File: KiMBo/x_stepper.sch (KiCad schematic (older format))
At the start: 11 parts

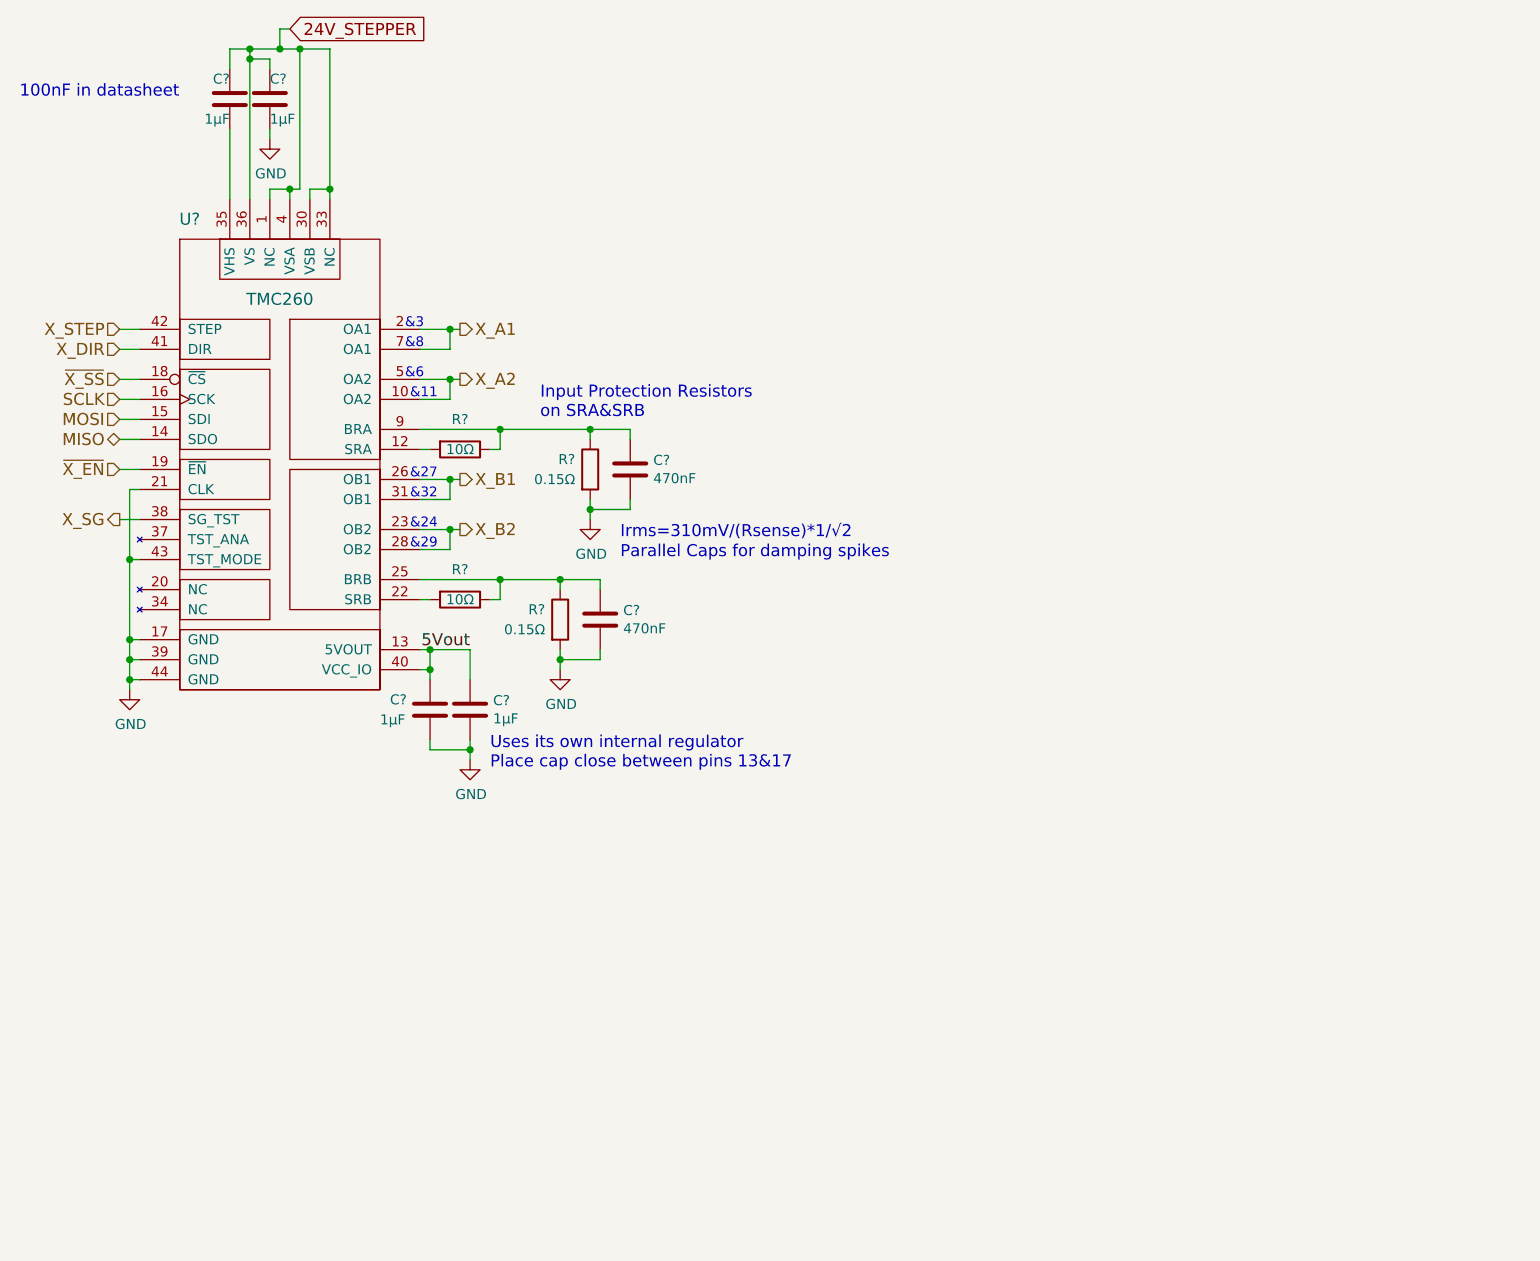
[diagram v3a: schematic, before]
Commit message: Update the fixed Vain voltage and begin placing connectors at the highest level (root) of the hierarchical sheet structure
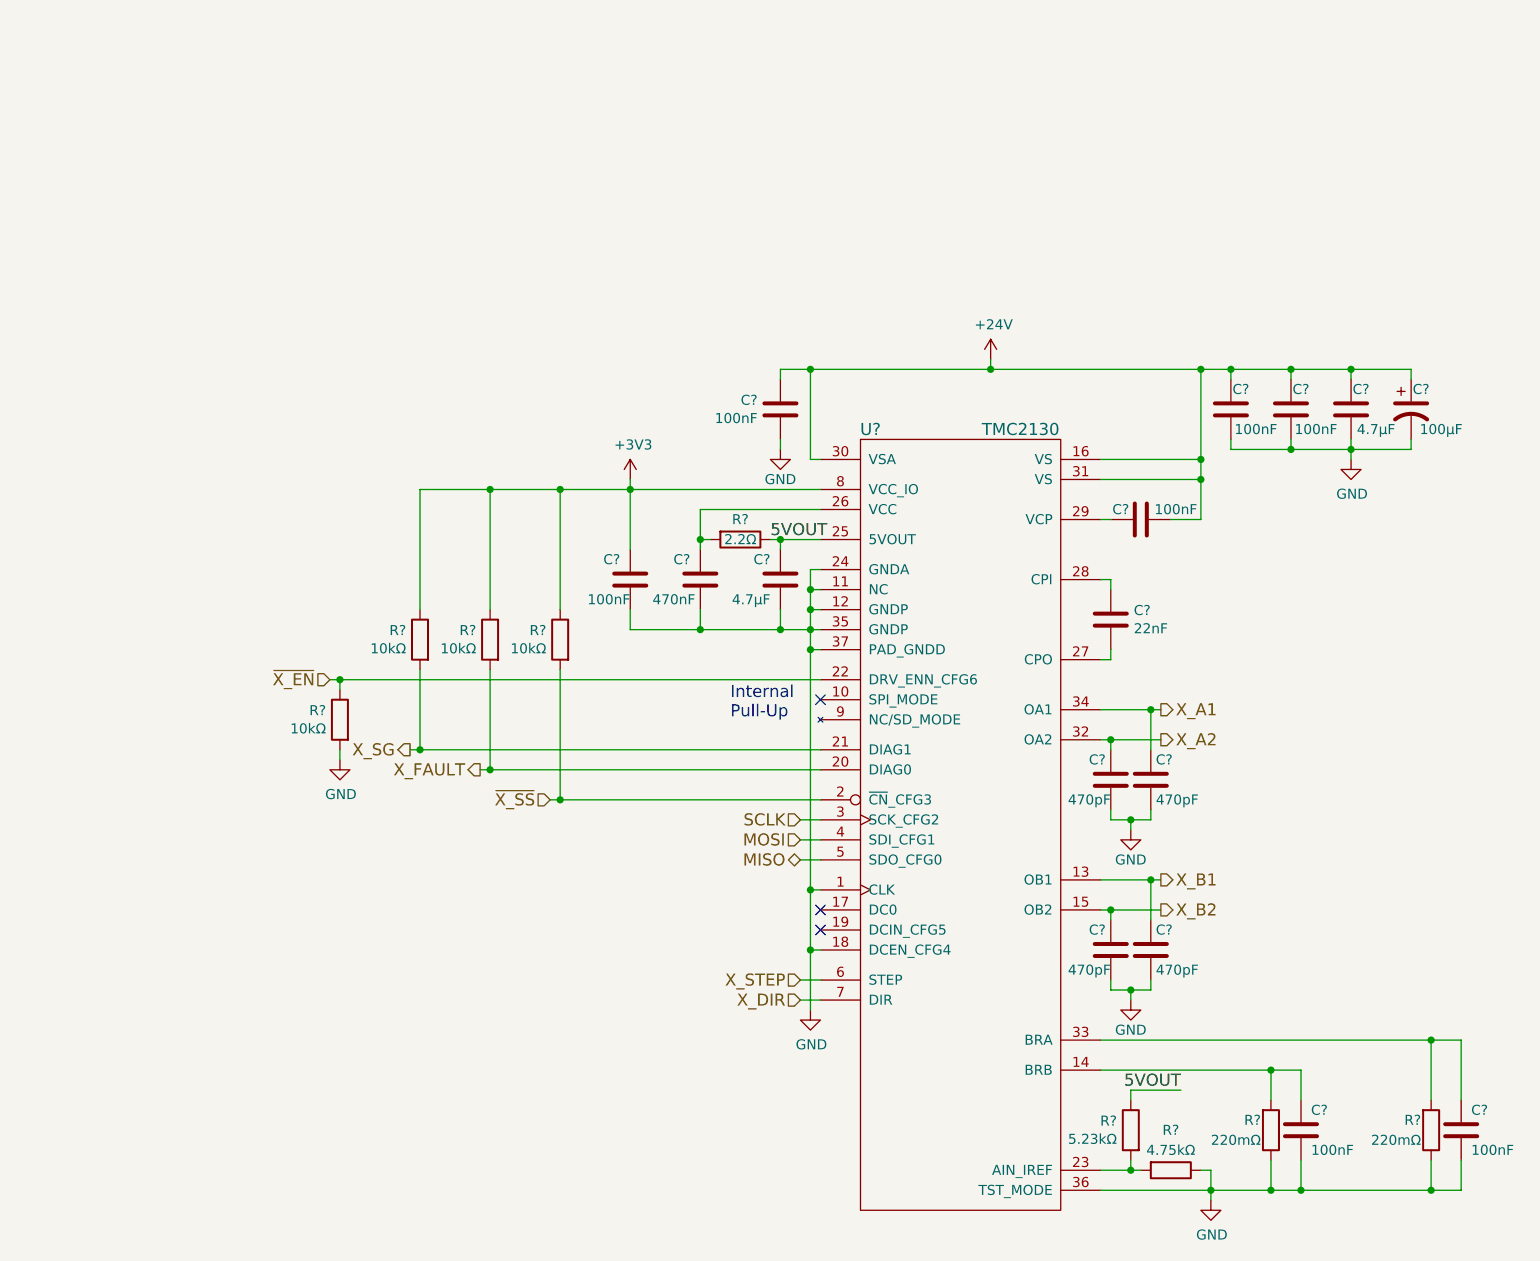
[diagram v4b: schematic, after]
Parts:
- removed C? (x4): 1μF, symbol C
- removed C? (x2): 470nF, symbol C
- removed R? (x2): 10Ω, symbol R
- removed R? (x2): 0.15Ω, symbol R
- removed U?: TMC260, KiMBo:LQFP-44-Trinamic_10x10mm_Pitch0.8mm, symbol TMC260
- added C? (x7): 100nF, symbol C
- added C?: 100μF, symbol CP1
- added C?: 22nF, symbol C
- added C?: 470nF, symbol C
- added C? (x2): 4.7μF, symbol C
- added C? (x4): 470pF, symbol C
- added R? (x2): 220mΩ, symbol R
- added R?: 2.2Ω, symbol R
- added R? (x4): 10kΩ, symbol R
- added R?: 5.23kΩ, symbol R
- added R?: 4.75kΩ, symbol R
- added U?: TMC2130, symbol TMC2130
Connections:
- net GND: now also C?.1, C?.2, C?.2, C?.2, C?.2, C?.2, C?.2, C?.2, C?.2, C?.2, C?.2, C?.2, C?.2, C?.2, R?.1, R?.1, R?.1, R?.2, U?.1 (CLK), U?.11 (NC), U?.12 (GNDP), U?.18 (DCEN_CFG4), U?.24 (GNDA), U?.35 (GNDP), U?.36 (TST_MODE), U?.37 (PAD_GNDD)
- net MISO: now also U?.5 (SDO_CFG0)
- net MOSI: now also U?.4 (SDI_CFG1)
- net SCLK: now also U?.3 (SCK_CFG2)
- net X_A1: now also C?.1, U?.34 (OA1)
- net X_A2: now also C?.1, U?.32 (OA2)
- net X_B1: now also C?.1, U?.13 (OB1)
- net X_B2: now also C?.1, U?.15 (OB2)
- net X_DIR: now also U?.7 (DIR)
- net X_SG: now also R?.2, U?.21 (DIAG1)
- net X_STEP: now also U?.6 (STEP)
- net ~X_EN: now also R?.1, U?.22 (DRV_ENN_CFG6)
- net ~X_SS: now also R?.2, U?.2 (~CN~_CFG3)
- new net: C?.2, U?.29 (VCP)
- new net: C?.1, U?.28 (CPI)
- new net: C?.2, U?.27 (CPO)
- new net: C?.1, R?.2, U?.33 (BRA)
- new net: C?.1, R?.2, U?.14 (BRB)
- new net: C?.1, R?.2, U?.26 (VCC)
- new net: R?.2, R?.2, U?.23 (AIN_IREF)
- new net +24V: C?.1, C?.1, C?.1, C?.1, C?.1, C?.2, U?.16 (VS), U?.30 (VSA), U?.31 (VS)
- new net +3V3: C?.1, R?.1, R?.1, R?.1, U?.8 (VCC_IO)
- new net 5VOUT: C?.1, R?.1, R?.1, U?.25 (5VOUT)
- new net X_FAULT: R?.2, U?.20 (DIAG0)
- no-connect marks 0 -> 3
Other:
- note added: "Internal\nPull-Up"
- note removed: "&11"
- note removed: "&24"
- note removed: "&27"
- note removed: "&29"
- note removed: "&3"
- note removed: "&32"
- note removed: "&6"
- note removed: "&8"
- note removed: "100nF in datasheet"
- note removed: "Input Protection Resistors\non SRA&SRB"
- note removed: "Irms=310mV/(Rsense)*1/√2"
- note removed: "Parallel Caps for damping spikes"
- note removed: "Uses its own internal regulator\nPlace cap close between pins 13&17"

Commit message: Create nodes for more SS, add H stepper, begin fixing power rail names
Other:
- note removed: "Internal\nPull-Up"
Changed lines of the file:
@@
 $Descr A3 16535 11693
 encoding utf-8
-Sheet 10 23
+Sheet 13 25
 Title ""
 Date ""
@@
 ~X_EN
 NoConn ~ 7700 4550
-Text Notes 7250 4650 0    60   ~ 0
-Internal\nPull-Up
-$Comp
-L C C?
+$Comp
+L C C?
